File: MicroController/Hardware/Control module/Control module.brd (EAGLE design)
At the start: 100 x 60 mm, 92 parts, among them CN1 JST-PH_2-PIN_HEADER, CN2 JST-PH_2-PIN_HEADER, CN3 JST-PH_2-PIN_HEADER, CN4 JST-PH_2-PIN_HEADER, CN5 JST-PH_2-PIN_HEADER, CN6 JST-PH_2-PIN_HEADER, CN7 JST-PH_2-PIN_HEADER, CN8 JST-PH_2-PIN_HEADER, J1 1X2-3.5MM, J2 RJ45-TRAFO, J3 RJ45-TRAFO, J4 RJ45-TRAFO, J6 RJ11, Q1 BSS138, Q2 BSS138, Q3 BSS138, Q4 BSS138, Q5 BSS138, Q6 BSS138, Q7 BSS138, Q8 BSS138, U1 CD74HC4067SM96, U2 DUAL-OPTOISOLATOR_SOIC8, U3 TLV1117-33CDCY, U4 DUAL-OPTOISOLATOR_SOIC8

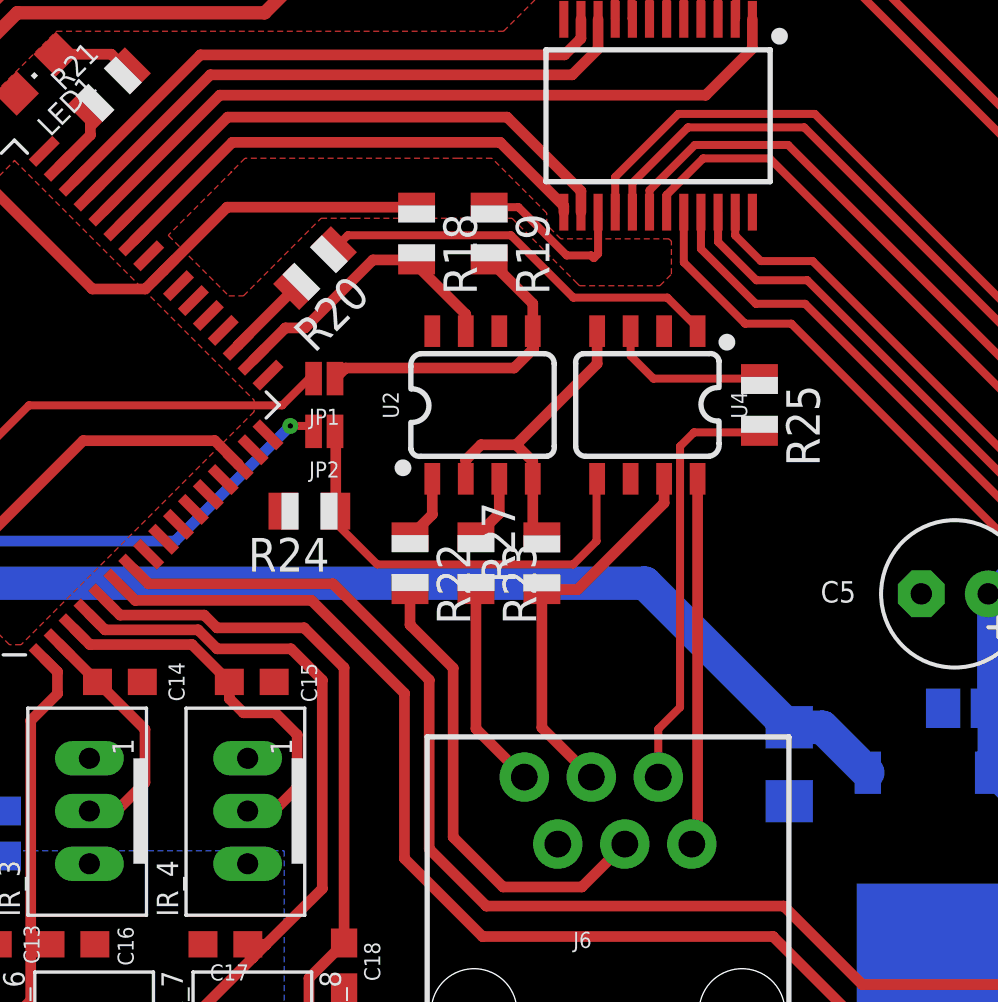
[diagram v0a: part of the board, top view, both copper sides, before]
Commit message: New project for the ultrasone sensor PCB.
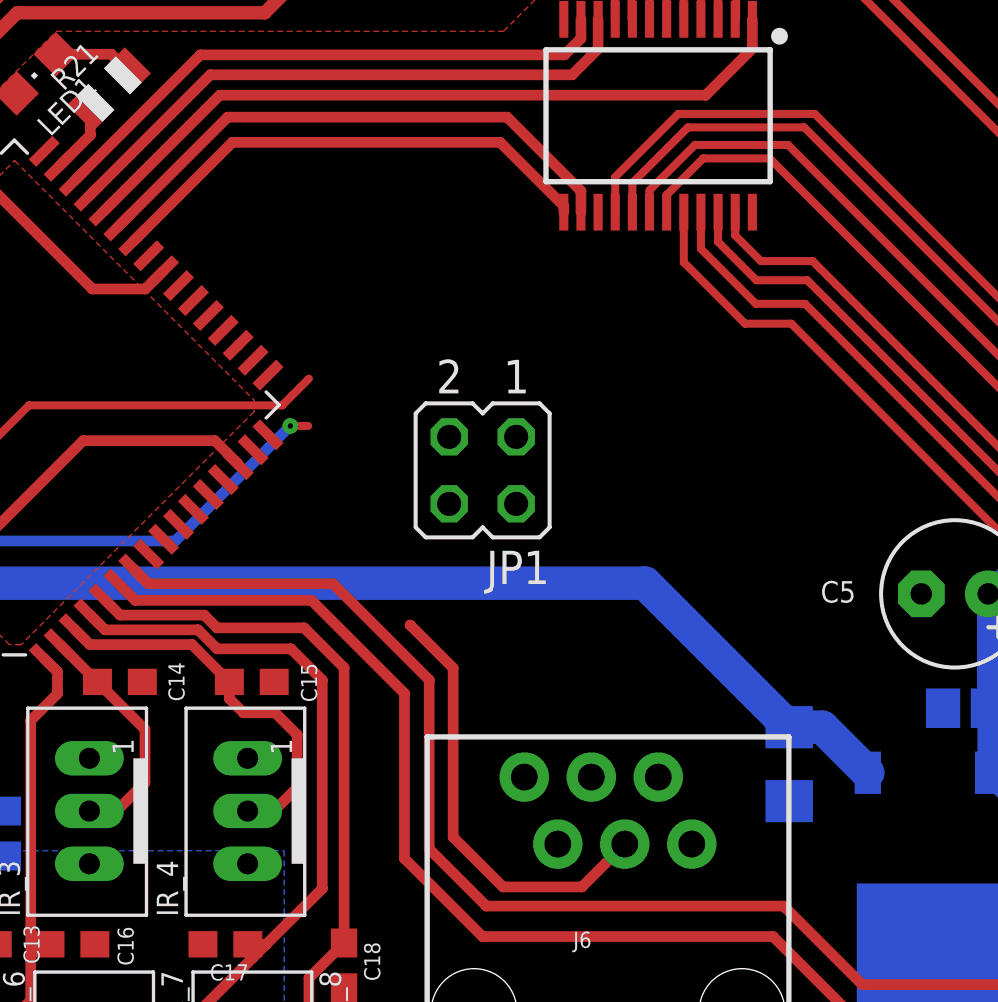
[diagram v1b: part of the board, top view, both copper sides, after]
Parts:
- removed JP2: JUMPER-SMT_2_NO_NO-SILK, SparkFun-Jumpers:SMT-JUMPER_2_NO_NO-SILK
- removed R18, R19, R20, R22, R23, R24, R25, R27: 10K, adafruit:R0805
- removed U2, U4: DUAL-OPTOISOLATOR_SOIC8, SparkFun-DiscreteSemi:SO08
- JP1: value JUMPER-SMT_2_NO_NO-SILK -> (none); device SparkFun-Jumpers:SMT-JUMPER_2_NO_NO-SILK -> jumper:JP2Q
- moved JP1 6.94 mm to (57.8, 27.5)
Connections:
- removed net N$2: JP1.1, R19.2, U2.5
- removed net N$4: R20.1, U4.1
- removed net N$5: R25.1, U4.3
- removed net N$6: R22.1, U2.1
- removed net N$7: R23.1, U2.3
- removed net N$8: JP2.1, R24.1, U4.5
- removed net RX_RASPI: J6.3, R27.1, U4.7
- removed net TX_RASPI: J6.4, R22.2
- net DATA_RASPI: now also JP1.2; no longer R25.2
- net GND: no longer R18.1, R19.1, R24.2, U4.2
- net GND_RASPI: no longer R27.2, U2.2, U2.4, U4.4
- net PDI_DATA: now also JP1.1; no longer JP2.2
- net RESET_PDI_CLK: now also JP1.3; no longer JP1.2
- net RES_RASPI: now also JP1.4; no longer R23.2
- net RX_ATXMEGA: now also J6.3; no longer R18.2, U2.7
- net TX_ATXMEGA: now also J6.4; no longer R20.2
- net VCC: no longer U2.6, U2.8, U4.6
- net VCC_RASPI: no longer U4.8
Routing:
- net TX_RASPI: track 18.0 -> 0.00 mm
- net GND: track 49.0 -> 31.8 mm
- net N$8: track 16.8 -> 0.00 mm
- net DATA_RASPI: track 16.1 -> 0.00 mm
- net N$4: track 15.6 -> 0.00 mm
- net RX_RASPI: track 14.8 -> 0.00 mm
- net VCC_RASPI: track 13.9 -> 0.31 mm
- net TX_ATXMEGA: track 3.14 -> 16.7 mm
- net GND_RASPI: track 12.3 -> 0.00 mm
- net N$2: track 12.1 -> 0.00 mm
- net RX_ATXMEGA: track 11.2 -> 0.00 mm
- net RES_RASPI: track 7.87 -> 0.00 mm
- net N$5: track 6.18 -> 0.00 mm
- net N$7: track 2.57 -> 0.00 mm
- net N$6: track 2.55 -> 0.00 mm

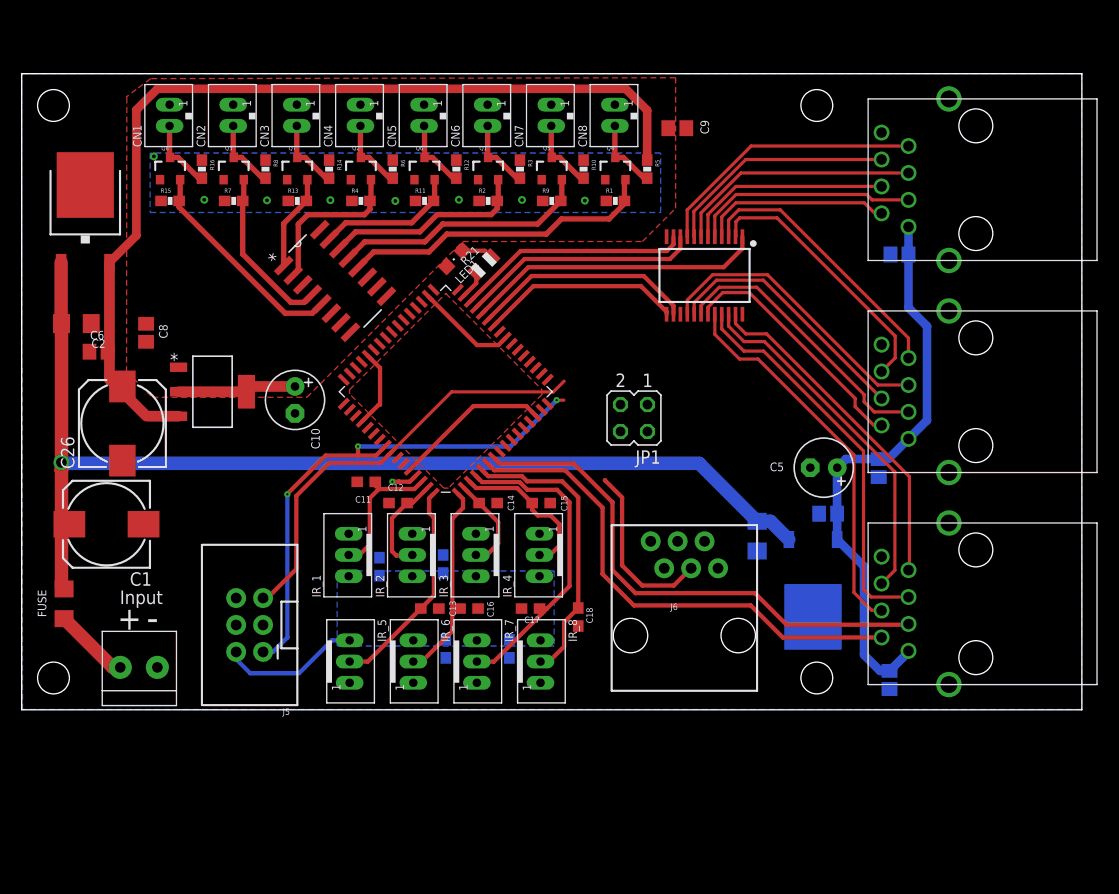
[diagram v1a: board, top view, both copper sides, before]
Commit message: Changed the layout drastically, especially the multiplexer.
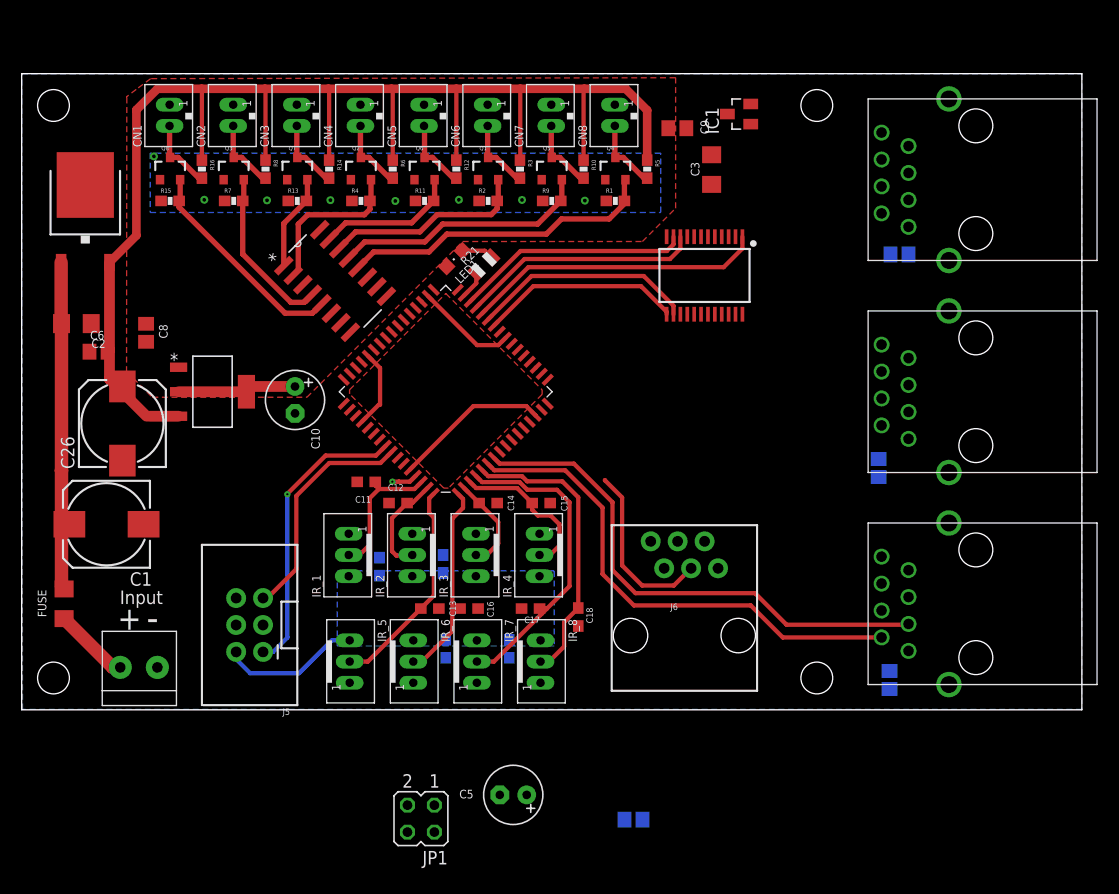
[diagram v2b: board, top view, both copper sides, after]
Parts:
- removed 5V_REGULATOR: 7805DT, adafruit:TO252
- added IC1: MCP1703CB, linear:SOT23
- moved JP1 42.8 mm to (37.7, -10.3)
- moved C5 42.6 mm to (46.4, -8.03)
- moved C3 34.8 mm to (65.1, 51.0), flipped to the top
- moved C7 34.2 mm to (57.7, -10.4)
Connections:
- net +12V: now also C25.1, C3.1, IC1.3, J2.8
- net +24V: no longer 5V_REGULATOR.1, C3.1
- net +5V: now also IC1.2; no longer 5V_REGULATOR.2, C25.1, J2.1
- net GND: now also IC1.1; no longer 5V_REGULATOR.3, J2.8
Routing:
- net +24V: track 104.2 -> 31.8 mm, vias 1 -> 0
- net +5V: track 53.7 -> 0.10 mm
- net +12V: track 89.7 -> 137.0 mm
- net ULTRA11: track 37.1 -> 0.00 mm
- net ULTRA12: track 36.0 -> 0.00 mm
- net ULTRA10: track 33.6 -> 0.00 mm
- net ULTRA9: track 32.1 -> 0.00 mm
- net ULTRA16: track 27.5 -> 0.00 mm
- net ULTRA14: track 26.4 -> 0.00 mm
- net ULTRA1: track 25.9 -> 0.00 mm
- net ULTRA7: track 25.8 -> 0.00 mm
- net ULTRA8: track 25.1 -> 0.00 mm
- net ULTRA15: track 24.3 -> 0.00 mm
- net ULTRA3: track 23.4 -> 0.00 mm
- net ULTRA13: track 23.2 -> 0.00 mm
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
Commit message: Major improvements
The Ultrasone PCB is in a good place now, it has also been well implemented on the control PCB.
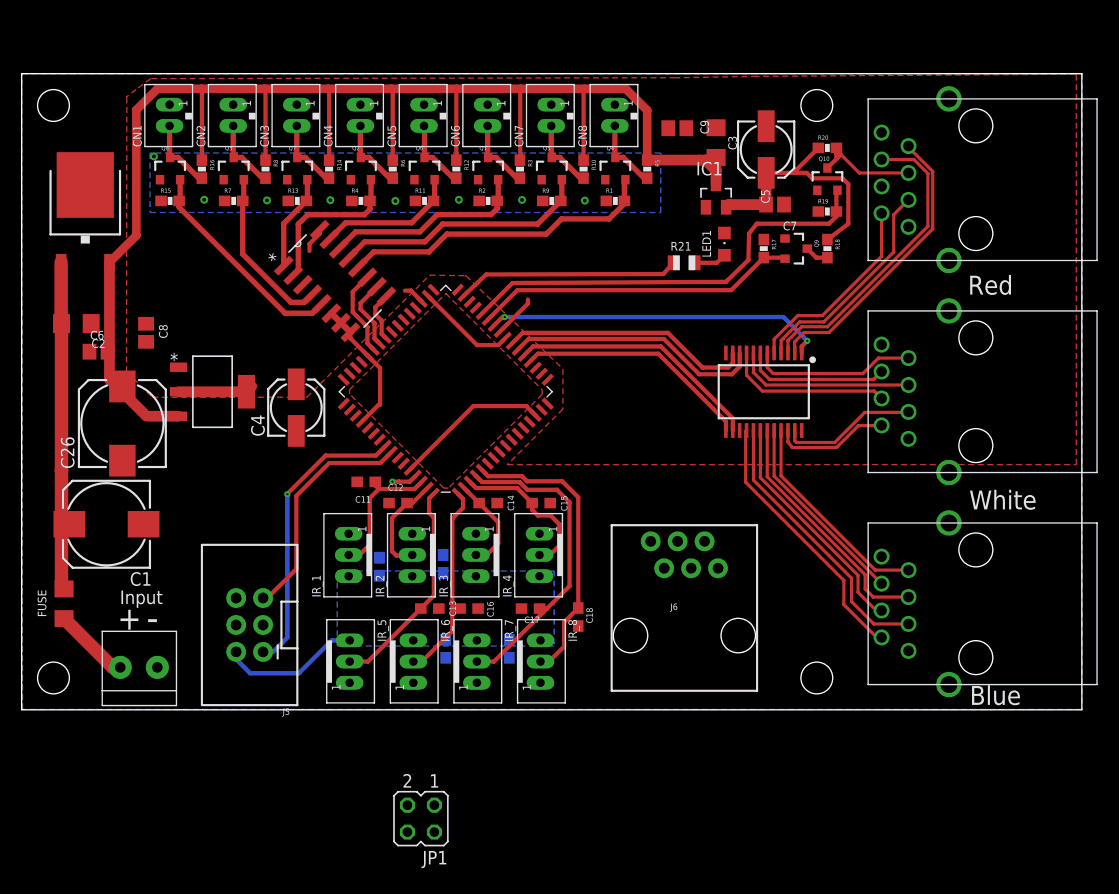
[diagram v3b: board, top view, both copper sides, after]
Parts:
- removed C10: (no value), adafruit:E2,5-6
- removed C23, C24, C25: (no value), adafruit:C0805
- added C4: (no value), adafruit:153CLV-0505
- added Q10, Q9: BSS138, SparkFun:SOT23-3
- added R17, R18, R19, R20: 10K, SparkFun:0603-RES
- C5: device adafruit:E2,5-6 -> adafruit:153CLV-0505
- moved C5 65.4 mm to (70.2, 52.8), turned to 270 degrees
- moved C7 59.5 mm to (71.1, 47.7), flipped to the top
- moved J4 40.0 mm to (90.0, 50.0)
- moved LED1 25.5 mm to (66.3, 43.9), turned to 0 degrees
- moved J2 20.0 mm to (90.0, 30.0)
- moved J3 20.0 mm to (90.0, 10.0)
- moved R21 18.9 mm to (62.5, 42.2), turned to 180 degrees
- moved U1 12.3 mm to (70.0, 30.0)
- moved IC1 7.99 mm to (65.5, 48.5), turned to 0 degrees
- moved C3 2.58 mm to (65.5, 53.5), turned to 90 degrees
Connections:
- new net ATXMEGA_TRIGGER_1: Q10.2, R19.2, U$1.28
- new net ATXMEGA_TRIGGER_2: Q9.2, R17.2, U$1.27
- net +12V: no longer C25.1, J2.8
- net +5V: now also R18.1, R20.1; no longer C23.1, C24.1, J3.1, J4.1
- net A: now also U$1.43
- net B: now also U$1.42
- net C: now also U$1.41
- net GND: now also C4.-, J2.1, J2.8, J3.1, J4.1; no longer C10.-, C23.2, C24.2, C25.2
- net S0: now also U$1.22; no longer U$1.29
- net S1: now also U$1.23; no longer U$1.30
- net S2: now also U$1.21; no longer U$1.27
- net S3: now also U$1.20; no longer U$1.26
- net TRIGGER_1: now also J4.5, Q10.3, R20.2; no longer J4.2, U$1.6
- net TRIGGER_2: now also J4.4, Q9.3, R18.2; no longer J4.3, U$1.7
- net ULTRA1: now also U1.6; no longer U1.9
- net ULTRA10: now also J4.2, U1.5; no longer J4.6, U1.22
- net ULTRA11: now also J3.7; no longer J4.5
- net ULTRA12: now also J3.6; no longer J4.4
- net ULTRA13: now also J3.5; no longer J3.2
- net ULTRA14: now also J3.4; no longer J3.3
- net ULTRA15: now also J3.3; no longer J3.4
- net ULTRA16: now also J3.2; no longer J3.5
- net ULTRA2: now also U1.7; no longer U1.8
- net ULTRA3: now also U1.8; no longer U1.7
- net ULTRA4: now also U1.9; no longer U1.6
- net ULTRA5: now also U1.23; no longer U1.5
- net ULTRA6: now also U1.22; no longer U1.4
- net ULTRA7: now also J4.7, U1.2; no longer J3.7, U1.3
- net ULTRA8: now also J4.6, U1.3; no longer J3.6, U1.2
- net ULTRA9: now also J4.3, U1.4; no longer J4.7, U1.23
- net ULTRA_COM: now also U$1.26; no longer U$1.28
- net VCC: now also C4.+, Q10.1, Q9.1, R17.1, R19.1; no longer C10.+
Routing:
- net TRIGGER_2: track 49.4 -> 2.25 mm
- net ATXMEGA_TRIGGER_1: track 0.00 -> 41.2 mm
- net TRIGGER_1: track 47.6 -> 11.0 mm
- net ATXMEGA_TRIGGER_2: track 0.00 -> 30.5 mm
- net ULTRA8: track 0.00 -> 28.7 mm
- net ULTRA7: track 0.00 -> 27.3 mm
- net ULTRA15: track 0.00 -> 26.2 mm
- net ULTRA16: track 0.00 -> 25.1 mm
- net +5V: track 0.10 -> 24.6 mm
- net ULTRA13: track 0.00 -> 23.2 mm
- net ULTRA14: track 0.00 -> 22.0 mm
- net ULTRA9: track 0.00 -> 20.8 mm
- net ULTRA11: track 0.00 -> 20.0 mm
- net ULTRA10: track 0.00 -> 18.7 mm
- net ULTRA12: track 0.00 -> 18.6 mm
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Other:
- board text added: "Blue"
- board text added: "Red"
- board text added: "White"

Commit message: Changed the Control PCB design to follow the Eurocircuits design rules.
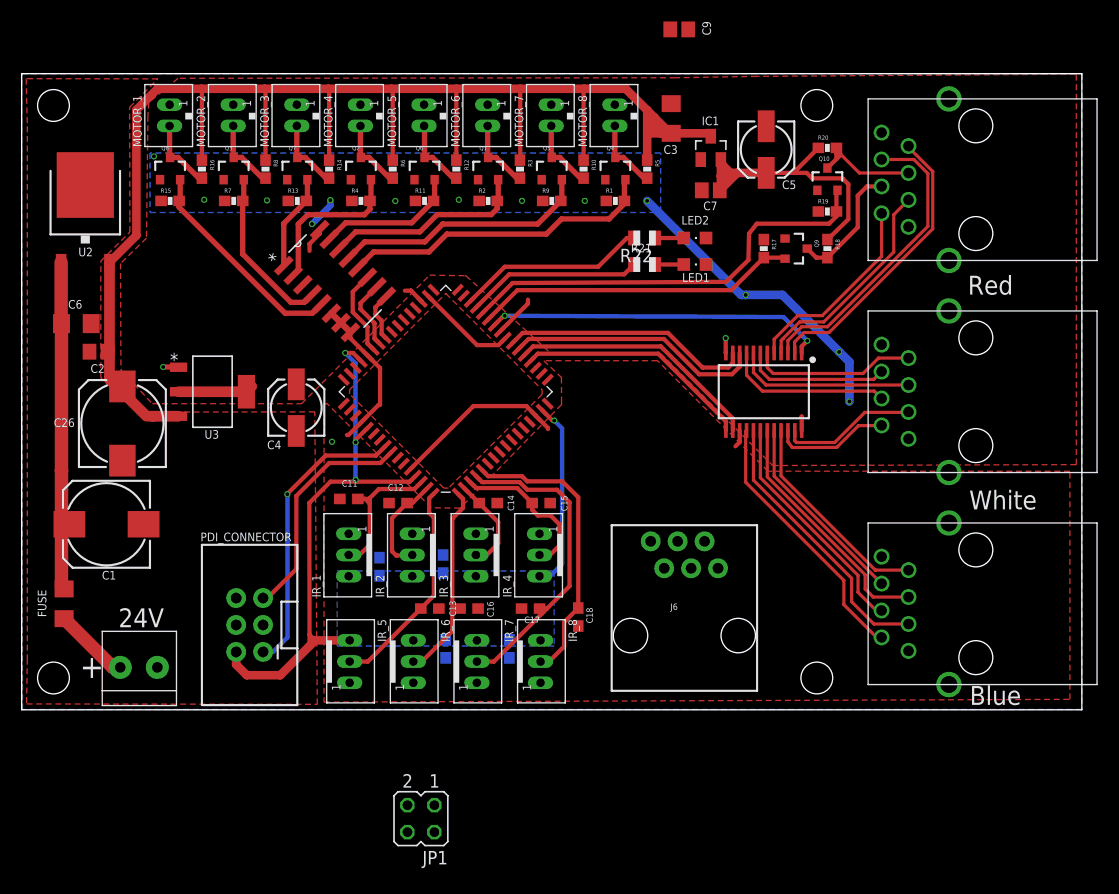
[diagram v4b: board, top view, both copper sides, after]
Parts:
- removed C8: (no value), adafruit:C0805
- added LED2: (no value), led:CHIPLED_0805
- added R22: 10K, adafruit:R0805
- moved C9 9.32 mm to (62.0, 64.2)
- moved C7 6.21 mm to (65.0, 49.0), turned to 180 degrees
- moved C3 4.81 mm to (61.3, 55.8)
- moved IC1 4.53 mm to (65.0, 53.0)
- moved R21 3.74 mm to (58.8, 42.0)
- moved LED1 3.38 mm to (63.5, 42.0), turned to 270 degrees
- moved C11 2.30 mm to (30.9, 19.9)
- renumbered 12V_REGULATOR to U2, CN1 to MOTOR_1, CN2 to MOTOR_2, CN3 to MOTOR_3, CN4 to MOTOR_4, CN5 to MOTOR_5, CN6 to MOTOR_6, CN7 to MOTOR_7, CN8 to MOTOR_8, J5 to PDI_CONNECTOR
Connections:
- new net LED_1: R21.2, U$1.29
- new net LED_2: R22.2, U$1.30
- net +12V: no longer C8.1
- net GND: now also LED2.C; no longer C8.2
- net N$1: now also LED2.A, R22.1; no longer R21.2, U$1.31
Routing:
- net VCC: track 31.4 -> 122.5 mm, vias 9 -> 17
- net N$1: track 21.1 -> 2.70 mm
- net LED_2: track 0.00 -> 18.0 mm
- net LED_1: track 0.00 -> 16.6 mm
- net TRIGGER_2: track 2.25 -> 11.9 mm
- net GND: track 37.2 -> 45.4 mm, vias 0 -> 3
- net +5V: track 24.6 -> 28.9 mm
- net IR_1: track 13.2 -> 14.8 mm
- net +12V: track 147.5 -> 148.1 mm
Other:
- board text added: "24V"
- board text removed: "-"
- board text removed: "Input"
